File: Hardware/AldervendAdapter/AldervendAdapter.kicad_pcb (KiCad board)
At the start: 2 copper layers, 85 x 60 mm, 40 parts, among them J101 MDB_MASTER, J102 MDB_SLAVE, J103 PROG, SW101 RESET, SW102 BOOT, U101 PC817, U102 PC817, U103 K7805M-1000R3, U104 AMS1117-3.3, U106 ESP32-C6-MINI-1

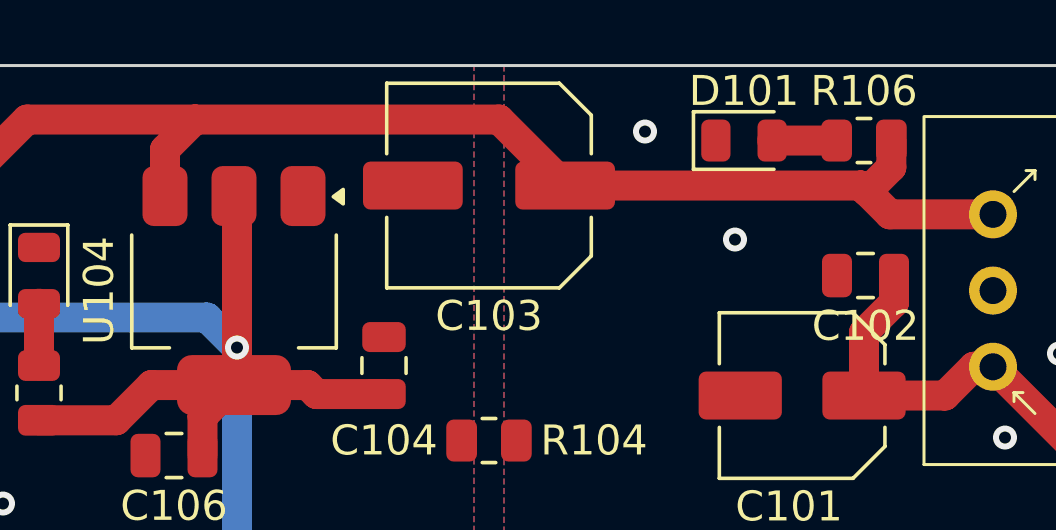
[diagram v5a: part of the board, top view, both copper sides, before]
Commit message: Find some replacement parts for standard assembly
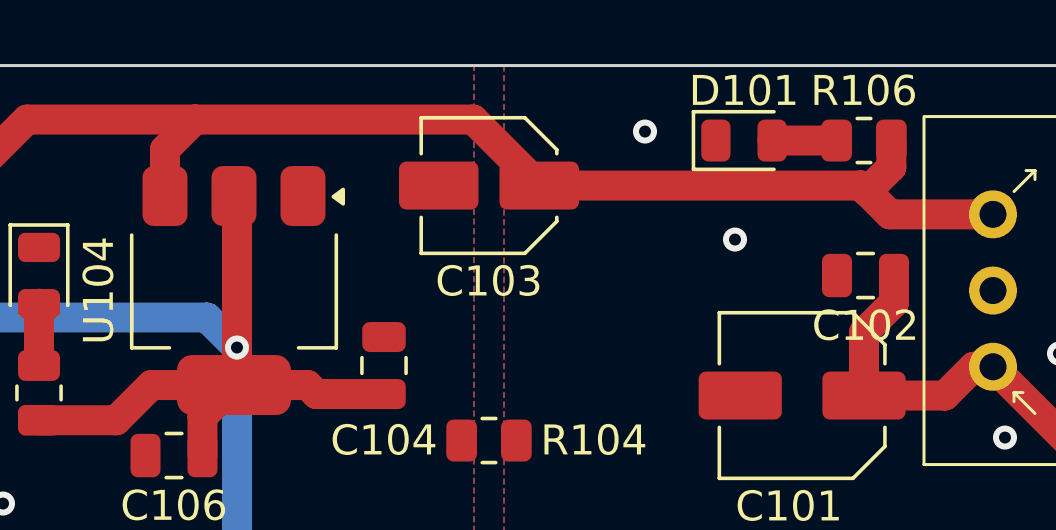
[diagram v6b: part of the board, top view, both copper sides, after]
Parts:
- C103: footprint Capacitor_SMD:C_Elec_6.3x5.4 -> Capacitor_SMD:C_Elec_4x5.4
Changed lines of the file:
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@@
 			)
 		)
-		(property "LCSC#" "C74622"
+		(property "LCSC#" "C27784"
 			(at 0 0 180)
 			(unlocked yes)
@@
 		)
 	)
-	(footprint "Capacitor_SMD:C_Elec_6.3x5.4"
+	(footprint "Capacitor_SMD:C_Elec_4x5.4"
 		(layer "F.Cu")
 		(at 191 74 180)
-		(descr "SMD capacitor, aluminum electrolytic nonpolar, 6.3x5.4mm")
+		(descr "SMD capacitor, aluminum electrolytic nonpolar, 4.0x5.4mm")
 		(tags "capacitor electrolytic nonpolar")
 		(property "Reference" "C103"
-			(at 0 -4.35 0)
+			(at 0 -3.2 180)
 			(layer "F.SilkS")
 			(effects
@@
 		)
 		(property "Value" "22uF"
-			(at 0 4.35 0)
+			(at 0 3.2 180)
 			(layer "F.Fab")
 			(effects
@@
 		)
 		(property "Datasheet" "~"
-			(at 0 0 0)
+			(at 0 0 180)
 			(layer "F.Fab")
 			(hide yes)
@@
 		)
 		(property "Description" "Unpolarized capacitor, small symbol"
-			(at 0 0 0)
+			(at 0 0 180)
 			(layer "F.Fab")
 			(hide yes)
@@
 			)
 		)
-		(property "LCSC#" "C72494"
+		(property "LCSC#" "C3356"
 			(at 0 0 180)
 			(unlocked yes)
@@
 		(attr smd)
 		(fp_line
-			(start 3.41 3.41)
-			(end 3.41 1.06)
+			(start 2.26 2.26)
+			(end 2.26 1.06)
 			(stroke
 				(width 0.12)
@@
 		)
 		(fp_line
-			(start 3.41 -3.41)
-			(end 3.41 -1.06)
+			(start 2.26 -2.26)
+			(end 2.26 -1.06)
 			(stroke
 				(width 0.12)
@@
 		)
 		(fp_line
-			(start -2.345563 3.41)
-			(end 3.41 3.41)
+			(start -1.195563 2.26)
+			(end 2.26 2.26)
 			(stroke
 				(width 0.12)
@@
 		)
 		(fp_line
-			(start -2.345563 -3.41)
-			(end 3.41 -3.41)
+			(start -1.195563 -2.26)
+			(end 2.26 -2.26)
 			(stroke
 				(width 0.12)
@@
 		)
 		(fp_line
-			(start -3.41 2.345563)
-			(end -2.345563 3.41)
+			(start -2.26 1.195563)
+			(end -1.195563 2.26)
 			(stroke
 				(width 0.12)
@@
 		)
 		(fp_line
-			(start -3.41 2.345563)
-			(end -3.41 1.06)
+			(start -2.26 1.195563)
+			(end -2.26 1.06)
 			(stroke
 				(width 0.12)
@@
 		)
 		(fp_line
-			(start -3.41 -2.345563)
-			(end -2.345563 -3.41)
+			(start -2.26 -1.195563)
+			(end -1.195563 -2.26)
 			(stroke
 				(width 0.12)
@@
 		)
 		(fp_line
-			(start -3.41 -2.345563)
-			(end -3.41 -1.06)
+			(start -2.26 -1.195563)
+			(end -2.26 -1.06)
 			(stroke
 				(width 0.12)
@@
 		)
 		(fp_line
-			(start 4.45 1.05)
-			(end 3.55 1.05)
+			(start 3.25 1.05)
+			(end 2.4 1.05)
 			(stroke
 				(width 0.05)
@@
 		)
 		(fp_line
-			(start 4.45 -1.05)
-			(end 4.45 1.05)
+			(start 3.25 -1.05)
+			(end 3.25 1.05)
 			(stroke
 				(width 0.05)
@@
 		)
 		(fp_line
-			(start 3.55 1.05)
-			(end 3.55 3.55)
+			(start 2.4 1.05)
+			(end 2.4 2.4)
 			(stroke
 				(width 0.05)
@@
 		)
 		(fp_line
-			(start 3.55 -1.05)
-			(end 4.45 -1.05)
+			(start 2.4 -1.05)
+			(end 3.25 -1.05)
 			(stroke
 				(width 0.05)
@@
 		)
 		(fp_line
-			(start 3.55 -3.55)
-			(end 3.55 -1.05)
+			(start 2.4 -2.4)
+			(end 2.4 -1.05)
 			(stroke
 				(width 0.05)
@@
 		)
 		(fp_line
-			(start -2.4 3.55)
-			(end 3.55 3.55)
+			(start -1.25 2.4)
+			(end 2.4 2.4)
 			(stroke
 				(width 0.05)
@@
 		)
 		(fp_line
-			(start -2.4 -3.55)
-			(end 3.55 -3.55)
+			(start -1.25 -2.4)
+			(end 2.4 -2.4)
 			(stroke
 				(width 0.05)
@@
 		)
 		(fp_line
-			(start -3.55 2.4)
-			(end -2.4 3.55)
+			(start -2.4 1.25)
+			(end -1.25 2.4)
 			(stroke
 				(width 0.05)
@@
 		)
 		(fp_line
-			(start -3.55 1.05)
-			(end -3.55 2.4)
+			(start -2.4 1.05)
+			(end -2.4 1.25)
 			(stroke
 				(width 0.05)
@@
 		)
 		(fp_line
-			(start -3.55 -1.05)
-			(end -4.45 -1.05)
+			(start -2.4 -1.05)
+			(end -3.25 -1.05)
 			(stroke
 				(width 0.05)
@@
 		)
 		(fp_line
-			(start -3.55 -2.4)
-			(end -2.4 -3.55)
+			(start -2.4 -1.25)
+			(end -1.25 -2.4)
 			(stroke
 				(width 0.05)
@@
 		)
 		(fp_line
-			(start -3.55 -2.4)
-			(end -3.55 -1.05)
+			(start -2.4 -1.25)
+			(end -2.4 -1.05)
 			(stroke
 				(width 0.05)
@@
 		)
 		(fp_line
-			(start -4.45 1.05)
-			(end -3.55 1.05)
+			(start -3.25 1.05)
+			(end -2.4 1.05)
 			(stroke
 				(width 0.05)
@@
 		)
 		(fp_line
-			(start -4.45 -1.05)
-			(end -4.45 1.05)
+			(start -3.25 -1.05)
+			(end -3.25 1.05)
 			(stroke
 				(width 0.05)
@@
 		)
 		(fp_line
-			(start 3.3 -3.3)
-			(end 3.3 3.3)
+			(start 2.15 -2.15)
+			(end 2.15 2.15)
 			(stroke
 				(width 0.1)
@@
 		)
 		(fp_line
-			(start -2.3 3.3)
-			(end 3.3 3.3)
+			(start -1.15 2.15)
+			(end 2.15 2.15)
 			(stroke
 				(width 0.1)
@@
 		)
 		(fp_line
-			(start -2.3 -3.3)
-			(end 3.3 -3.3)
+			(start -1.15 -2.15)
+			(end 2.15 -2.15)
 			(stroke
 				(width 0.1)
@@
 		)
 		(fp_line
-			(start -3.3 2.3)
-			(end -2.3 3.3)
+			(start -2.15 1.15)
+			(end -1.15 2.15)
 			(stroke
 				(width 0.1)
@@
 		)
 		(fp_line
-			(start -3.3 -2.3)
-			(end -2.3 -3.3)
+			(start -2.15 -1.15)
+			(end -1.15 -2.15)
 			(stroke
 				(width 0.1)
@@
 		)
 		(fp_line
-			(start -3.3 -2.3)
-			(end -3.3 2.3)
+			(start -2.15 -1.15)
+			(end -2.15 1.15)
 			(stroke
 				(width 0.1)
@@
 		(fp_circle
 			(center 0 0)
-			(end 3.15 0)
+			(end 2 0)
 			(stroke
 				(width 0.1)
@@
 		)
 		(fp_text user "${REFERENCE}"
-			(at 0 0 0)
+			(at 0 0 180)
 			(layer "F.Fab")
 			(effects
 				(font
-					(size 1 1)
-					(thickness 0.15)
+					(size 0.8 0.8)
+					(thickness 0.12)
 				)
 			)
 		)
 		(pad "1" smd roundrect
-			(at -2.5375 0 180)
-			(size 3.325 1.6)
+			(at -1.675 0 180)
+			(size 2.65 1.6)
 			(layers "F.Cu" "F.Mask" "F.Paste")
 			(roundrect_rratio 0.15625)
@@
 		)
 		(pad "2" smd roundrect
-			(at 2.5375 0 180)
-			(size 3.325 1.6)
+			(at 1.675 0 180)
+			(size 2.65 1.6)
 			(layers "F.Cu" "F.Mask" "F.Paste")
 			(roundrect_rratio 0.15625)
@@
 		)
 		(embedded_fonts no)
-		(model "${KICAD9_3DMODEL_DIR}/Capacitor_SMD.3dshapes/C_Elec_6.3x5.4.step"
+		(model "${KICAD9_3DMODEL_DIR}/Capacitor_SMD.3dshapes/C_Elec_4x5.4.step"
 			(offset
 				(xyz 0 0 0)
@@
 	)
 	(segment
-		(start 191.3375 71.8)
-		(end 193.5375 74)
+		(start 172.6 80)
+		(end 172.6 74.8)
 		(width 1)
 		(layer "F.Cu")
@@
 	)
 	(segment
-		(start 172.6 80)
-		(end 172.6 74.8)
+		(start 180.2 74.35)
+		(end 180.2 72.8)
 		(width 1)
 		(layer "F.Cu")
@@
 	)
 	(segment
-		(start 180.2 74.35)
-		(end 180.2 72.8)
+		(start 181.2 71.8)
+		(end 190.475 71.8)
+		(width 1)
+		(layer "F.Cu")
+		(net 4)
+	)
+	(segment
+		(start 192.675 74)
+		(end 203.4 74)
 		(width 1)
 		(layer "F.Cu")
@@
 	)
 	(segment
-		(start 203.4 74)
-		(end 193.5375 74)
+		(start 190.475 71.8)
+		(end 192.675 74)
 		(width 1)
 		(layer "F.Cu")
@@
 		(width 1)
 		(layer "F.Cu")
-		(net 4)
-	)
-	(segment
-		(start 181.2 71.8)
-		(end 191.3375 71.8)
-		(width 1)
-		(layer "F.Cu")

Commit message: last
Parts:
- added REF**: OSHW-Logo2_7.3x6mm_SilkScreen, Symbol:OSHW-Logo2_7.3x6mm_SilkScreen, B.Cu at (213.0, 122.4)
- added REF**: KiCad-Logo2_5mm_SilkScreen, Symbol:KiCad-Logo2_5mm_SilkScreen, B.Cu at (203.0, 122.0)
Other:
- outline, holes or cut-outs redrawn
- board text added: "${FULL_REVISION}"
- board text added: "-Julio"
- board text added: "Boot"
- board text added: "JLCJLCJLCJLC"
- board text added: "Master"
- board text added: "PROTOTYPE"
- board text added: "Reset"
- board text added: "Slave"
- board text added: "https://aldervon.com/"
- board text added: "https://github.com/Aldervon-Systems/AldervendAdapter/"
- board text added: "x D+ x 5v D- GND"
- board text added: "{dblquote}Juice{dblquote}"
